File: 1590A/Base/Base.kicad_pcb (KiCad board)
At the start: 2 copper layers, 32 x 67 mm, 50 parts, among them J101 Barrel_Jack_Switch, J102 AudioJack2_Ground, J103 AudioJack2_Ground, J104 Conn_01x04_Pin, J105 Conn_01x04_Pin, J106 Conn_01x04_Pin, Q101 DMC3071LVT, Q102 BC846, Q201 LS844, Q301 DMC3071LVT, Q302 DMC3071LVT, Q303 DMC3071LVT

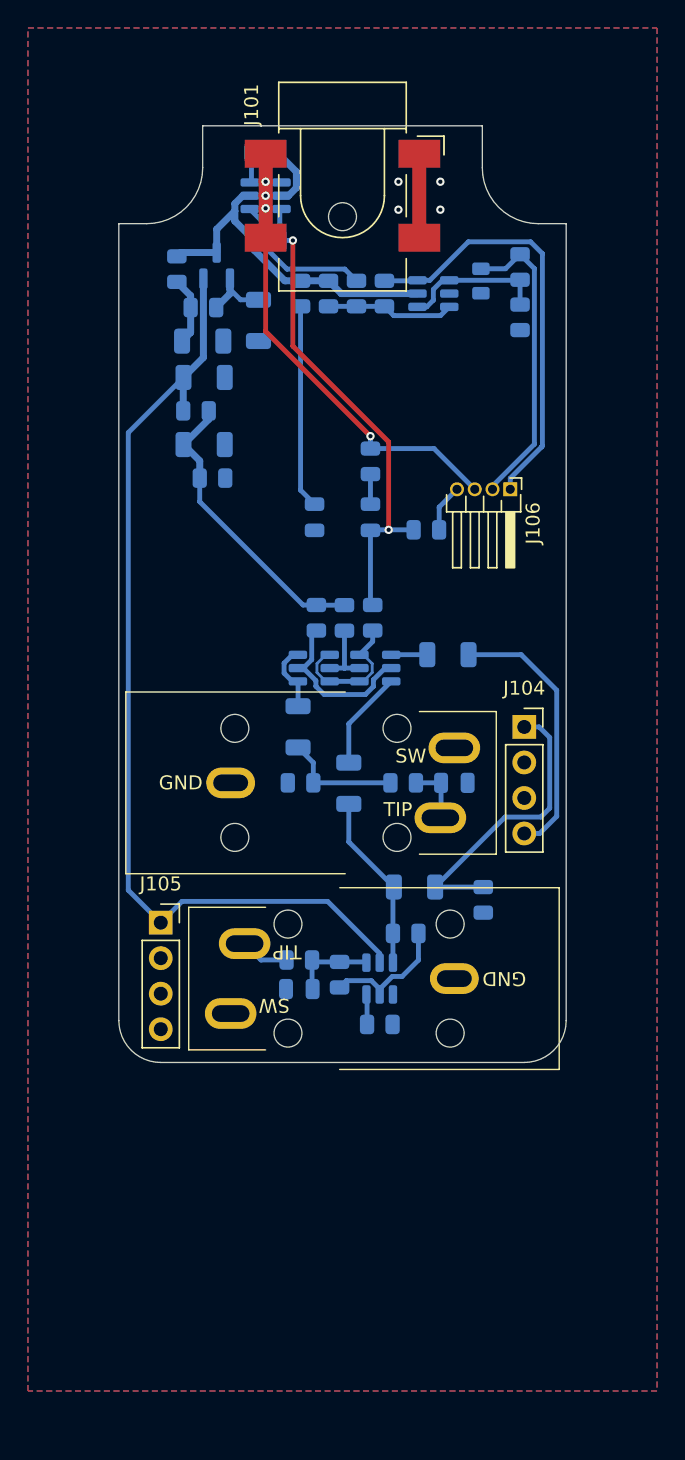
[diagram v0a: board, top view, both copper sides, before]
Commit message: Update 1590A board
I really wanted to use the stomp switch board, but I didn't find any
sane connectors that are convenient and fit.

So I just updated this board to have the stomp switch directly on the
board instead.  I'd love to re-use stomp switches after I have made a
(bad) design and tested it, but the pain just doesn't seem worth it.

That means that I could just have used a traditional latching 3PDT, but
instead this sticks to the electronic switching with a momentary switch.
Because the whole point is the circuit, not sanity.

Add another openscad 3d model for this stomp switch thing.

Signed-off-by: Linus Torvalds <torvalds@linux-foundation.org>
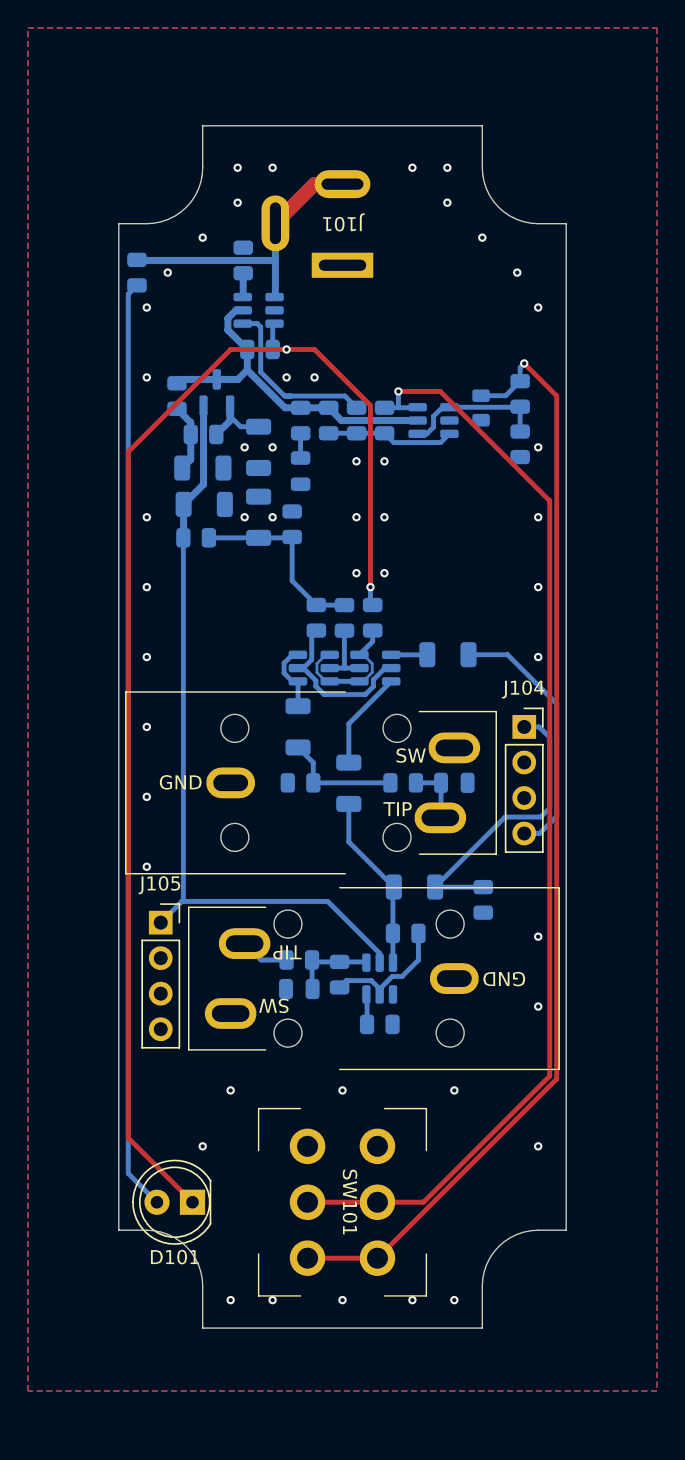
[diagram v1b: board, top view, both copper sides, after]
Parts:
- removed the D102 at (102.0, 85.0)
- removed J106: Conn_01x04_Pin, Connector_PinHeader_1.27mm:PinHeader_1x04_P1.27mm_Horizontal
- removed the R105 at (102.0, 81.0)
- removed R108: 2k2, Resistor_SMD:R_0805_2012Metric
- added D101: LED, LED_THT:LED_D5.0mm, F.Cu at (89.3, 134.0)
- added R104: 2k2, Resistor_SMD:R_0805_2012Metric, B.Cu at (85.3, 67.5)
- added SW101: Stomp Switch, Mylib:FS5700DPMT2B2M2QE, F.Cu at (100.0, 134.0)
- J101: footprint Connector_BarrelJack:BarrelJack_CLIFF_FC681465S_SMT_Horizontal -> Mylib:Wurth WR-DC 2.1mm Power Jack
- moved C306 9.08 mm to (109.9, 77.2)
- moved R310 9.08 mm to (112.7, 76.2)
- moved C101 9.08 mm to (90.0, 81.5)
- moved C102 9.08 mm to (94.0, 80.0)
- moved C103 9.08 mm to (90.1, 84.1)
- moved Q102 9.08 mm to (91.0, 76.1)
- moved Q303 9.08 mm to (106.5, 78.1)
- moved R102 9.08 mm to (101.0, 78.1)
- moved R105 9.08 mm to (97.0, 78.1)
- moved R106 9.08 mm to (88.2, 76.3)
- moved R107 9.08 mm to (90.1, 79.1)
- moved R306 9.08 mm to (89.5, 86.5)
- moved R308 9.08 mm to (99.0, 78.1)
- moved R309 9.08 mm to (103.0, 78.1)
- moved R311 9.08 mm to (112.7, 79.8)
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- renumbered D101 to D102, R104 to R105, R312 to R311
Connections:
- J105 pad 4: LED -> unconnected-(J105-Pin_4-Pad4)
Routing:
- net Net-(D101-A): track 0.00 -> 66.7 mm
- net ON_LOW: track 35.3 -> 94.8 mm
- net SW2: track 21.7 -> 79.9 mm, vias 0 -> 1
- net SW1: track 30.6 -> 79.8 mm, vias 0 -> 1
- net +VA: track 70.1 -> 54.6 mm
- net Net-(D102-A): track 14.6 -> 1.77 mm
- net GND: track 10.4 -> 0.00 mm, vias 4 -> 47
- net PWRIN: track 35.9 -> 27.2 mm, vias 4 -> 0
- net VBIAS: track 21.1 -> 13.6 mm
- net Net-(J106-Pin_4): track 3.43 -> 0.00 mm
- net Net-(D102-A) (its old number): track 2.15 -> 0.00 mm
- net Net-(Q101A-G): track 10.7 -> 12.8 mm
- net OUT^{EFF}: track 19.2 -> 18.6 mm
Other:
- board size 32 x 67 mm -> 32 x 86 mm
- board text added: "PWR"
- board text removed: "ACT PWR"

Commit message: Another try at cleaning up project path handling
The removed TOPLEVEL hackery also tried to deal with the problem of
finding the spice models for simulation, which had the same confusion
with project-specific files and no sane kicad model that I could find
for it.

This attempts to deal with it by just making a 'spice' symlink from the
"kicad project" directory to the "real project" directory, and dealing
with the spice model paths that way.

Signed-off-by: Linus Torvalds <torvalds@linux-foundation.org>
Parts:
- removed Q102: BC846, Package_TO_SOT_SMD:SOT-23
- added Q1: BC846, Package_TO_SOT_SMD:SOT-23, B.Cu at (91.0, 76.0)

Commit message: Don't DC-couple the LS844 JFET input
I didn't think this through: it looks superficially fine only because
the circuit doesn't make the _other_ side of the JFET gate connection
obvious.

Without the AC-coupling capacitor, the input gate of the LS844 now has a
relatively low impedance path to ground, going through the instrument.
So the self-biasing to ground with a high-value resistor doesn't work at
all.

To do DC coupling, I'd need an actual negative rail.  I technically knew
that, but I clearly hadn't really internalized it and so just overlooked
this obvious (in hindsight) fact entirely.

I do have the simulation infrastructure for this and when you look at
the results you see that the biasing is all wrong without the
DC-blocking capacitor in place.

But to see that you do need to look at it, and I hadn't bothered since
it all used to work fine and I didn't think about this.

Signed-off-by: Linus Torvalds <torvalds@linux-foundation.org>
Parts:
- added C201: 4.7uF, Capacitor_SMD:C_1206_3216Metric, B.Cu at (92.4, 118.0)
- added R201: 1MEG, Resistor_SMD:R_0805_2012Metric, B.Cu at (89.7, 114.9)
- renumbered C201 to C202, C202 to C203, R201 to R202, R202 to R203, R203 to R204, R204 to R205, R205 to R206
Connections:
- R202 pad 1: IN^{CONN} -> Net-(C201-Pad2)
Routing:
- net IN^{CONN}: track 3.48 -> 7.29 mm
- net Net-(C201-Pad2): track 0.00 -> 2.89 mm

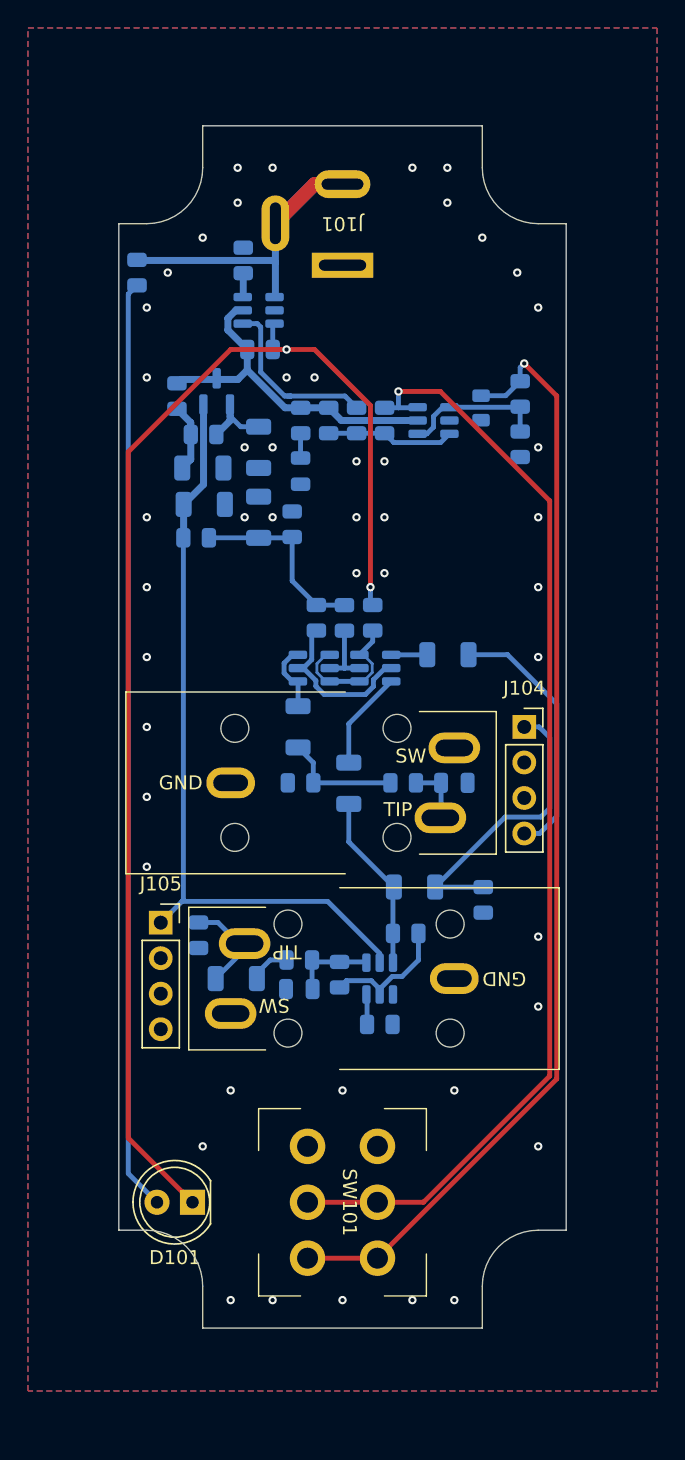
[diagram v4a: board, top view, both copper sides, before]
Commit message: 1590A: Replace the compact footswitch with a regular sized one
The bigger one probably fits better, since we have to reach up past the
audio jacks anyway.

I suspect I will go back to the actual 3PDT true bypass model for this
board, though.  The electronic switching is more interesting, but let's
face it, the simpler circuit with a physical switching of the signal is
simply more practical.

Signed-off-by: Linus Torvalds <torvalds@linux-foundation.org>
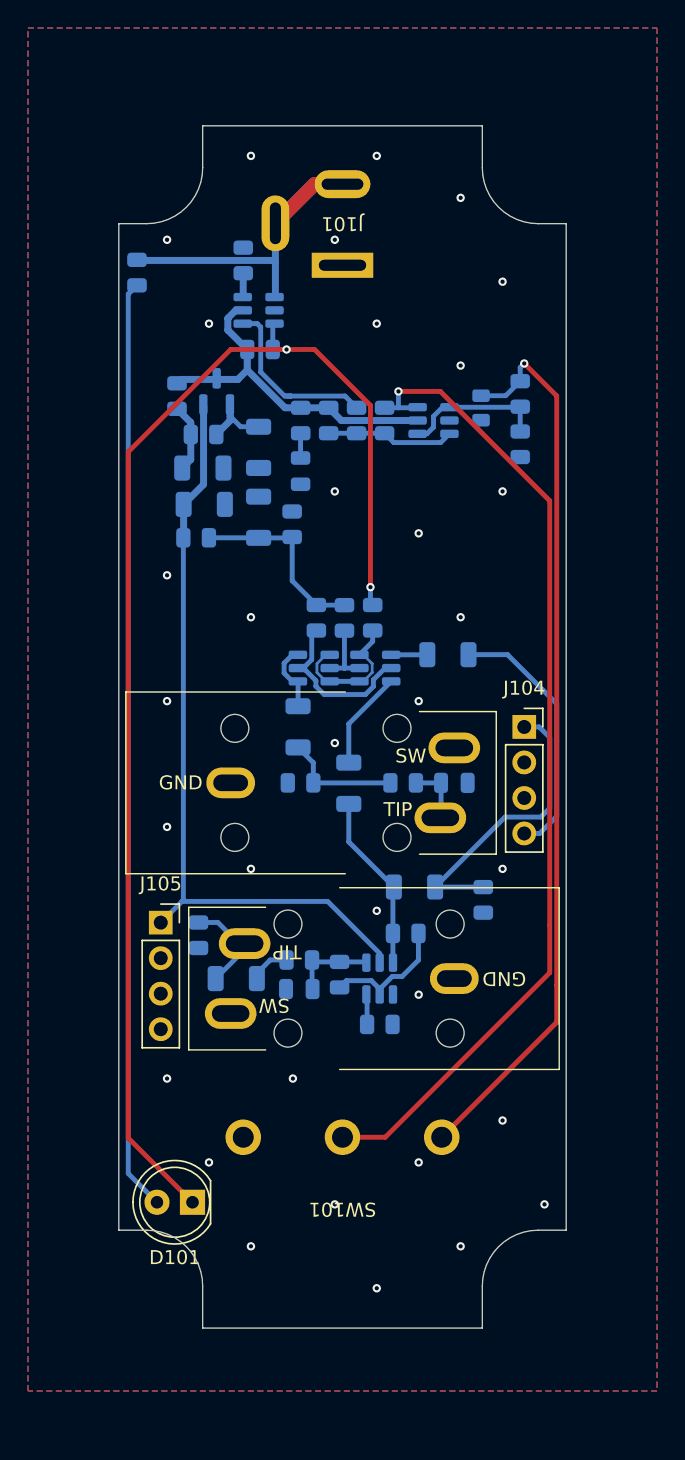
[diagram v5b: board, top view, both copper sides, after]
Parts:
- SW101: value Stomp Switch -> SW_Push_SPDT; footprint Mylib:FS5700DPMT2B2M2QE -> Mylib:PBS-24-102P
- turned SW101 to 180 degrees
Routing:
- net SW2: track 79.9 -> 64.3 mm
- net SW1: track 79.8 -> 71.1 mm
- net GND: vias 47 -> 33
